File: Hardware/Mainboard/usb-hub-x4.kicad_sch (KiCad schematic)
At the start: 1 part, among them IC2 TUSB2046BIRHBR

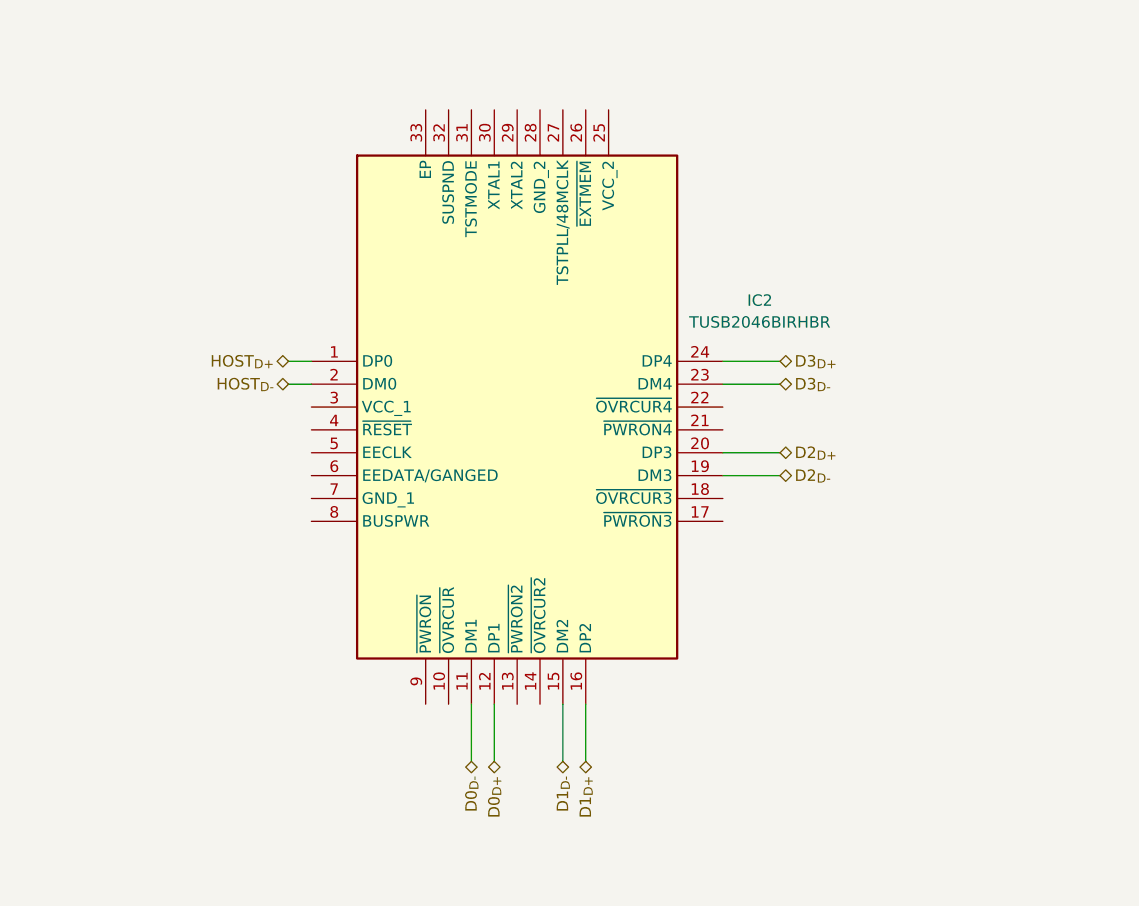
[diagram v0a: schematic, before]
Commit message: Adds RP2350 Stamp XL and dummy expansion board
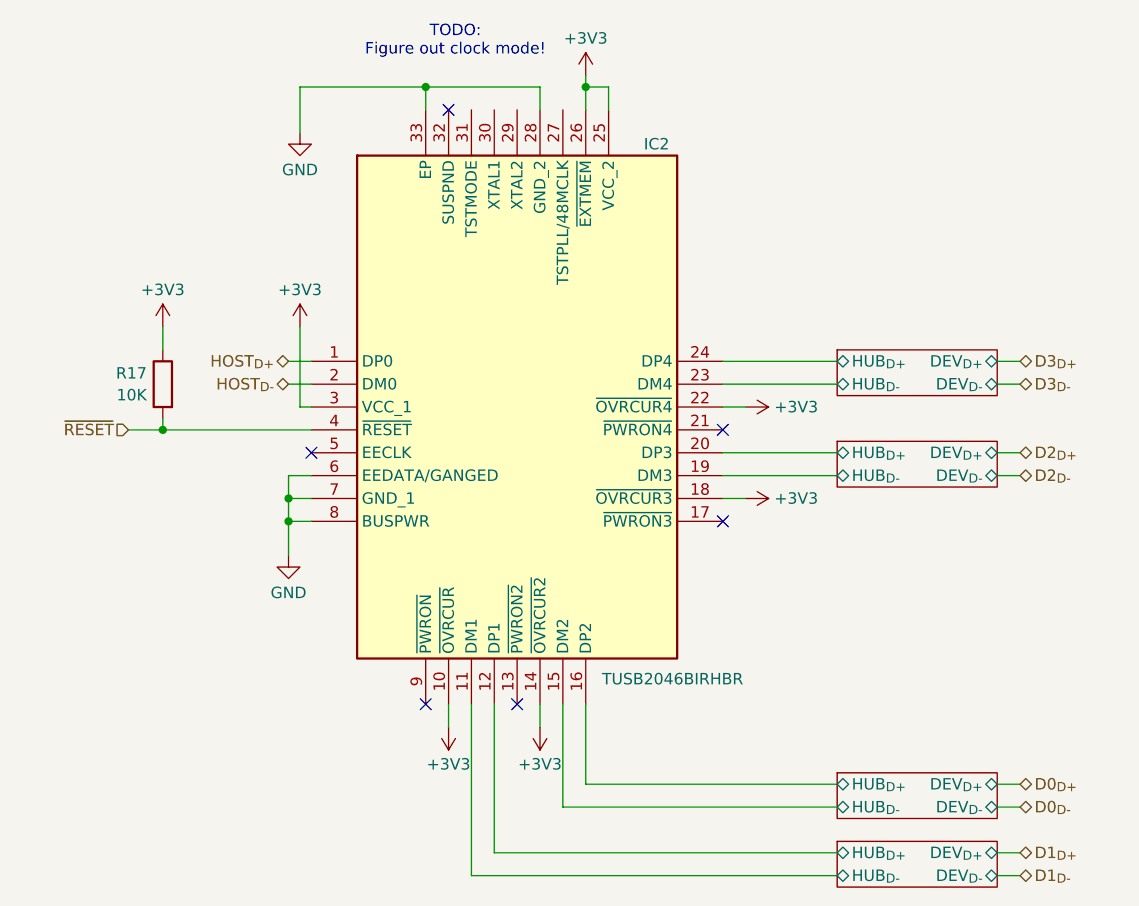
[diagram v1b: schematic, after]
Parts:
- added R17: 10K, Resistor_SMD:R_0603_1608Metric_Pad0.98x0.95mm_HandSolder, symbol Device:R
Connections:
- net D0_{D+}: no longer IC2.12 (DP1)
- net D0_{D-}: no longer IC2.11 (DM1)
- net D1_{D+}: no longer IC2.16 (DP2)
- net D1_{D-}: no longer IC2.15 (DM2)
- net D2_{D+}: no longer IC2.20 (DP3)
- net D2_{D-}: no longer IC2.19 (DM3)
- net D3_{D+}: no longer IC2.24 (DP4)
- net D3_{D-}: no longer IC2.23 (DM4)
- net +3V3: now reaches IC2.10 (~{OVRCUR})
- net +3V3: now also IC2.14 (~{OVRCUR2}), IC2.18 (~{OVRCUR3}), IC2.22 (~{OVRCUR4}), IC2.25 (VCC_2), IC2.26 (~{EXTMEM}), IC2.3 (VCC_1), R17.1
- net GND: now reaches IC2.28 (GND_2)
- net GND: now also IC2.33 (EP), IC2.6 (EEDATA/GANGED), IC2.7 (GND_1), IC2.8 (BUSPWR)
- net ~{RESET}: now reaches IC2.4 (~{RESET})
- net ~{RESET}: now also R17.2
- new net USB Terminator/HUB_{D+}: IC2.24 (DP4)
- new net USB Terminator/HUB_{D-}: IC2.23 (DM4)
- new net USB Terminator1/HUB_{D+}: IC2.20 (DP3)
- new net USB Terminator1/HUB_{D-}: IC2.19 (DM3)
- new net USB Terminator2/HUB_{D+}: IC2.16 (DP2)
- new net USB Terminator2/HUB_{D-}: IC2.15 (DM2)
- new net USB Terminator3/HUB_{D+}: IC2.12 (DP1)
- new net USB Terminator3/HUB_{D-}: IC2.11 (DM1)
- no-connect marks 0 -> 6
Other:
- added sheet USB Terminator (usb-port-terminator.kicad_sch)
- added sheet USB Terminator1 (usb-port-terminator.kicad_sch)
- added sheet USB Terminator2 (usb-port-terminator.kicad_sch)
- added sheet USB Terminator3 (usb-port-terminator.kicad_sch)
- note added: "TODO: Figure out clock mode!"
